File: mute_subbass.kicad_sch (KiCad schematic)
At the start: 16 parts, among them U4 LTC2909ITS8-2.5, U5 ADG5412FBRUZ

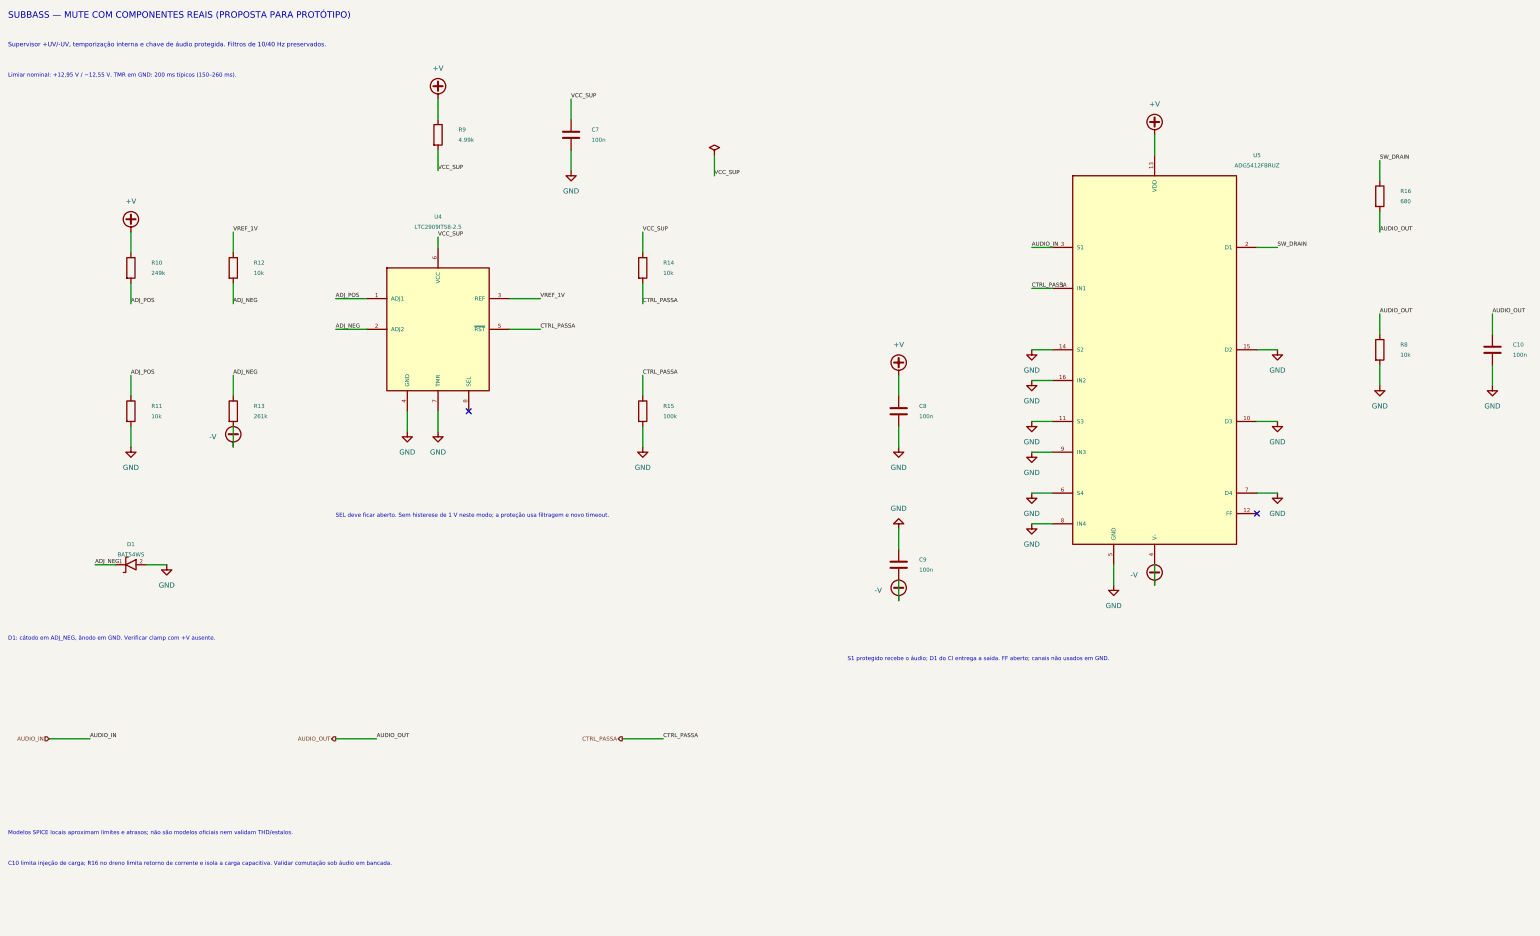
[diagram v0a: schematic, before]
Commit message: Refactor SubBass hardware and verification scripts for HW2 mute proposal
- Added TLV1702 fast fault path model to subbass_hardware.lib for improved fault detection.
- Updated plot_subbass.py title and descriptions to reflect changes in hardware proposal from HW1 to HW2.
- Modified verify_subbass.py to validate the new HW2 mute proposal, including adjustments to expected cutoff timing and report details.
- Enhanced test cases for fault detection and recovery scenarios to ensure robustness with new hardware configurations.
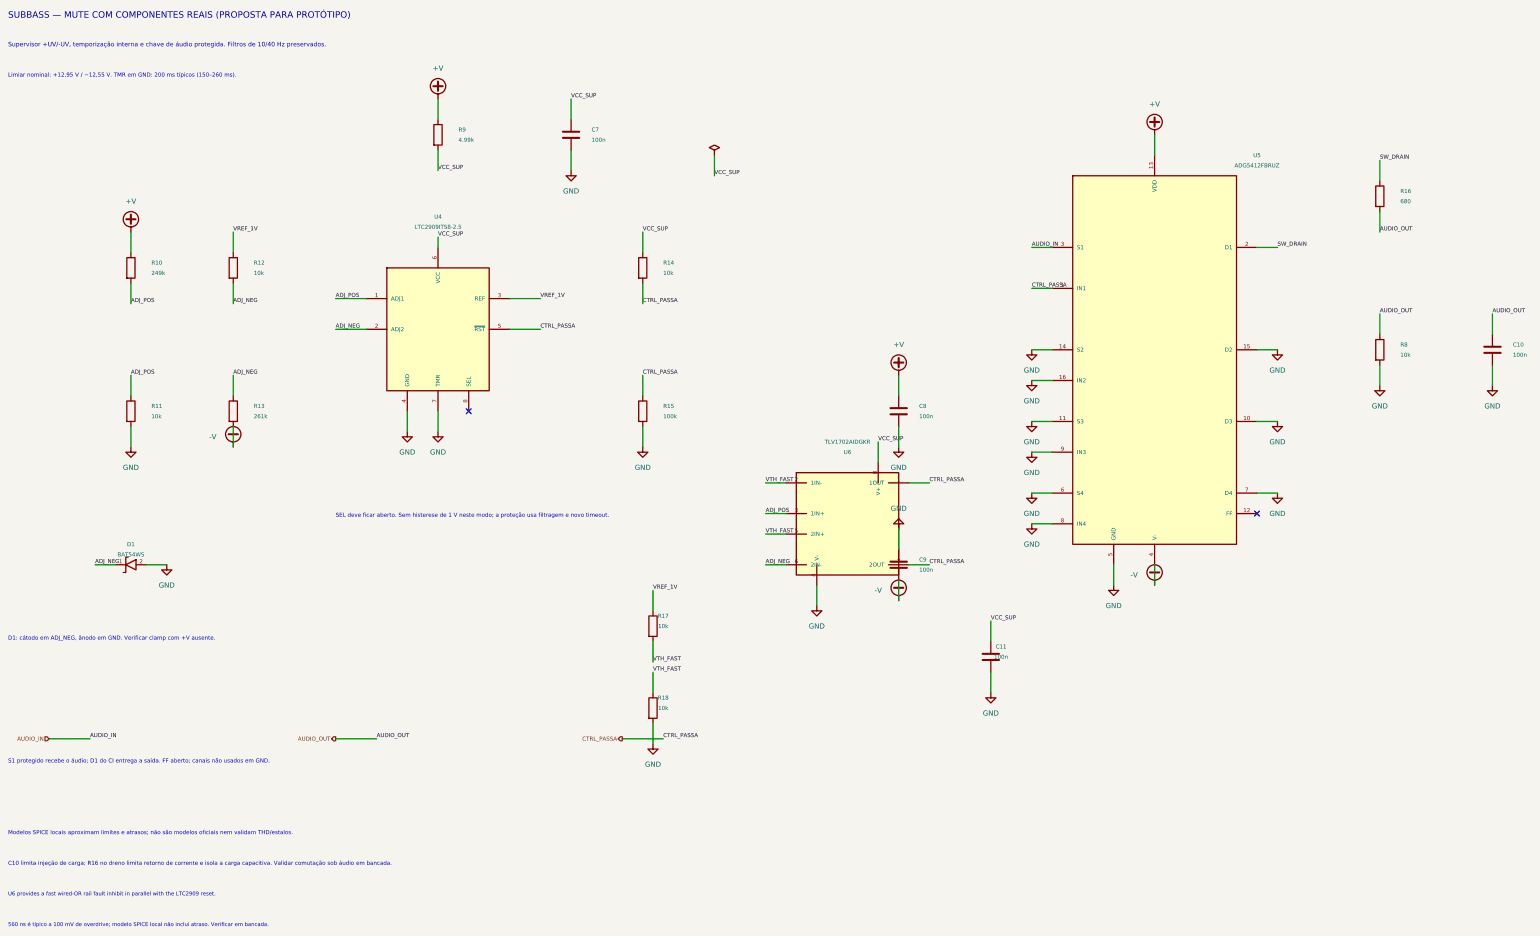
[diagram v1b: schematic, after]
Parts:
- added C11: 100n, Capacitor_SMD:C_0805_2012Metric, symbol Device:C
- added R17, R18: 10k, Resistor_SMD:R_0805_2012Metric, symbol Device:R
- added U6: TLV1702AIDGKR, Package_SO:VSSOP-8_2.3x2mm_P0.5mm, symbol Audio_HiFi:TLV1702AIDGKR
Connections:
- net ADJ_NEG: now also U6.6 (2IN-)
- net ADJ_POS: now also U6.3 (1IN+)
- net CTRL_PASSA: now also U6.1 (1OUT), U6.7 (2OUT)
- net GND: now also C11.2, R18.2, U6.4 (V-)
- net VCC_SUP: now also C11.1, U6.8 (V+)
- net VREF_1V: now also R17.1
- new net VTH_FAST: R17.2, R18.1, U6.2 (1IN-), U6.5 (2IN+)
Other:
- note added: "560 ns é típico a 100 mV de overdrive; modelo SPICE local não inclui atraso. Verificar em bancada."
- note added: "U6 provides a fast wired-OR rail fault inhibit in parallel with the LTC2909 reset."

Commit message: Ajustes e limpeza
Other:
- note removed: "560 ns é típico a 100 mV de overdrive; modelo SPICE local não inclui atraso. Verificar em bancada."
- note removed: "C10 limita injeção de carga; R16 no dreno limita retorno de corrente e isola a carga capacitiva. Validar comutação sob áudio em bancada."
- note removed: "D1: cátodo em ADJ_NEG, ânodo em GND. Verificar clamp com +V ausente."
- note removed: "Modelos SPICE locais aproximam limites e atrasos; não são modelos oficiais nem validam THD/estalos."
- note removed: "S1 protegido recebe o áudio; D1 do CI entrega a saída. FF aberto; canais não usados em GND."
- note removed: "SEL deve ficar aberto. Sem histerese de 1 V neste modo; a proteção usa filtragem e novo timeout."
- note removed: "U6 provides a fast wired-OR rail fault inhibit in parallel with the LTC2909 reset."
